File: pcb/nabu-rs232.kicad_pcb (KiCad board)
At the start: 2 copper layers, 119.4 x 58.4 mm, 30 parts, among them J1 NABU expansion slot, J2 TTL, J3 RS232, U1 74LS139, U2 74LS32, U3 74HCT04, U4 74HCT244, U5 8251, U6 74LS245, U7 8253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

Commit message: version 0.1 sent to jlcpcb
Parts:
- added J4: RS232 enable, Connector_PinHeader_2.54mm:PinHeader_2x03_P2.54mm_Vertical, F.Cu at (133.1, 119.4)
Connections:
- U8 pad 12: /RXD -> Net-(U8-Pad12)
- U9 pad 12: Net-(U5-Pad22) -> Net-(U9-Pad12)
- U9 pad 9: /CTS -> Net-(U9-Pad9)
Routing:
- net Net-(U8-Pad12): track 0.00 -> 43.8 mm, vias 0 -> 2
- net Net-(U9-Pad9): track 0.00 -> 30.6 mm, vias 0 -> 2
- net Net-(U5-Pad22): track 46.1 -> 72.1 mm, vias 2 -> 3
- net Net-(U9-Pad12): track 0.00 -> 20.4 mm
- net /CTS: track 59.0 -> 76.9 mm, vias 3 -> 2
- net GND: track 119.5 -> 129.0 mm, vias 11 -> 16
- net /RXD: track 112.3 -> 120.8 mm
- net /D7: track 35.7 -> 38.7 mm
- net /A0: track 100.0 -> 102.9 mm
- net /RESET: track 49.8 -> 52.7 mm
- net /CLK: track 126.1 -> 123.3 mm
- net VCC: track 276.9 -> 274.5 mm, vias 13 -> 14
- net /D0: track 43.6 -> 45.4 mm
- net /TXD: track 81.7 -> 83.4 mm
- net Net-(J3-Pad2): track 44.4 -> 46.1 mm
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
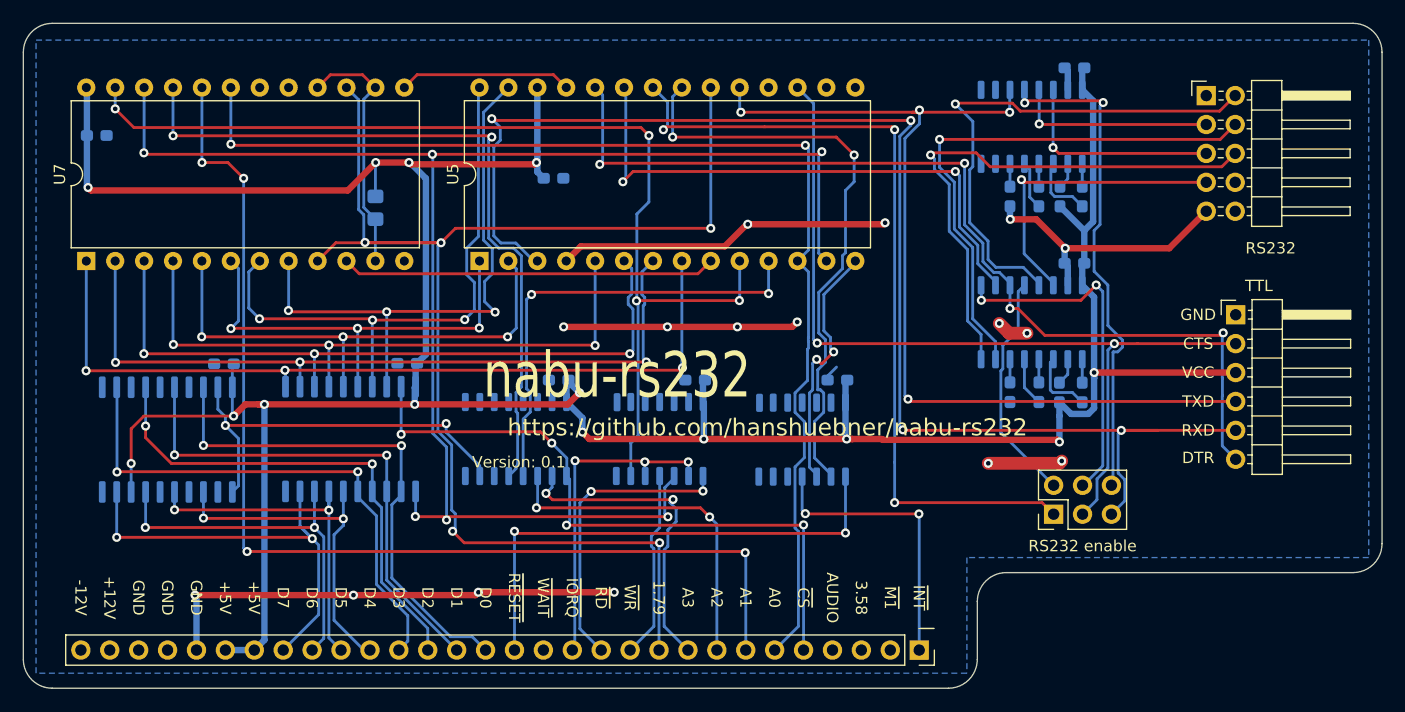
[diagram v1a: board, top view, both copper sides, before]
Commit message: Use proper DB9 RS232 pinout
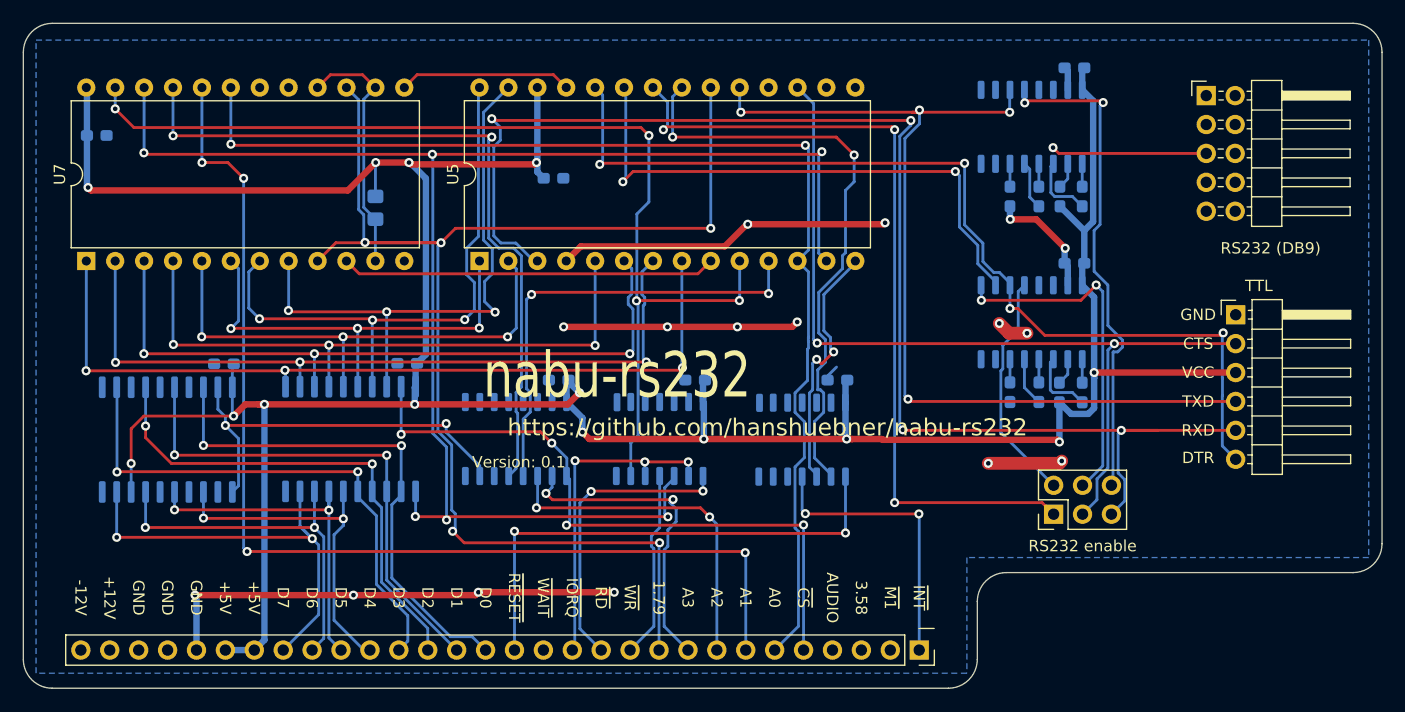
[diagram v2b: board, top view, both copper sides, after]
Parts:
- J3: value RS232 -> RS232 (DB9)
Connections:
- J3 pad 2: Net-(J3-Pad2) -> Net-(U8-Pad13)
- J3 pad 3: Net-(J3-Pad3) -> Net-(U8-Pad14)
- J3 pad 4: Net-(J3-Pad4) -> Net-(U9-Pad14)
- J3 pad 5: Net-(J3-Pad5) -> GND
- J3 pad 6: Net-(J3-Pad6) -> Net-(U9-Pad13)
- J3 pad 7: Net-(J3-Pad7) -> Net-(U9-Pad7)
- J3 pad 8: unconnected-(J3-Pad8) -> Net-(U9-Pad8)
- J3 pad 9: GND -> unconnected-(J3-Pad9)
- U8 pad 13: Net-(J3-Pad3) -> Net-(U8-Pad13)
- U8 pad 14: Net-(J3-Pad5) -> Net-(U8-Pad14)
- U9 pad 13: Net-(J3-Pad2) -> Net-(U9-Pad13)
- U9 pad 14: Net-(J3-Pad7) -> Net-(U9-Pad14)
- U9 pad 7: Net-(J3-Pad4) -> Net-(U9-Pad7)
- U9 pad 8: Net-(J3-Pad6) -> Net-(U9-Pad8)
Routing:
- net Net-(J3-Pad4): track 47.9 -> 0.00 mm, vias 1 -> 0
- net Net-(J3-Pad6): track 47.6 -> 0.00 mm, vias 1 -> 0
- net Net-(J3-Pad2): track 46.1 -> 0.00 mm, vias 1 -> 0
- net Net-(J3-Pad7): track 26.8 -> 0.00 mm, vias 1 -> 0
- net Net-(J3-Pad5): track 18.8 -> 0.00 mm, vias 1 -> 0
- net Net-(J3-Pad3): track 17.7 -> 0.00 mm, vias 1 -> 0
- net GND: track 129.0 -> 128.9 mm, vias 16 -> 17
